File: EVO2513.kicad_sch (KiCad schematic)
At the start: 0 parts

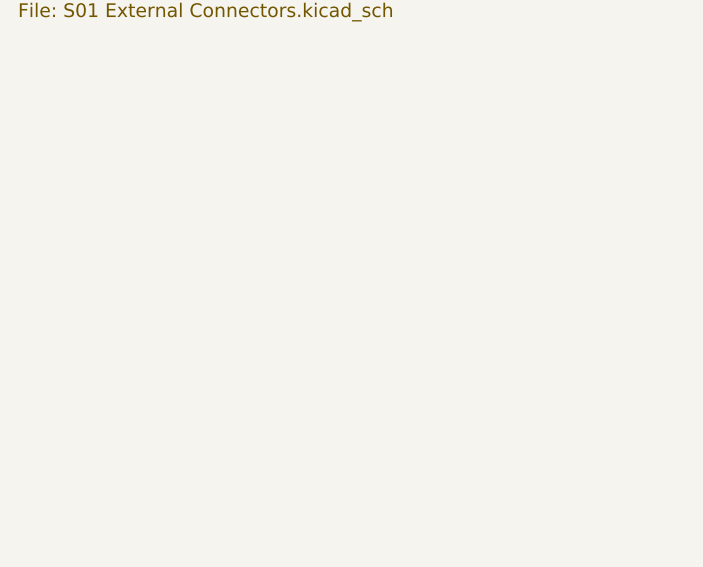
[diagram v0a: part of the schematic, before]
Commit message: Gate resistors placed, snubbers at the low-side FETs in EVM order, H1/H2/LOGO01 symbols
- R111-R114 (3R 0603) placed and routed next to the Q16-Q19 gates, each fed
  from In6 through a via in its driver-side pad.
- Snubbers reordered to match TI's LM51772EVM-HP (switch node -> C -> R -> GND)
  and moved to the low-side FETs: C39 on Q19's drain edge with R45 to GND,
  C35 on Q17's drain leads with R41 to GND, two In1 vias at each R GND pad.
  The top-copper SW1/SW2 pour lobes for the old positions are removed.
- H1, H2 (Mechanical:MountingHole_Pad, pin 1 to GND) and LOGO01 (pinless
  EVOSONIC_LOGO symbol) added to the root sheet and linked to their existing
  footprints, so Update PCB from Schematic no longer deletes them. The
  mounting-hole footprint is saved as MountingHole_3.2mm_Pad_7.4mm.
- ERC 0; DRC 0 unconnected, 0 parity, no courtyard overlaps.

Co-Authored-By: Claude Opus 5.5 <noreply@anthropic.com>
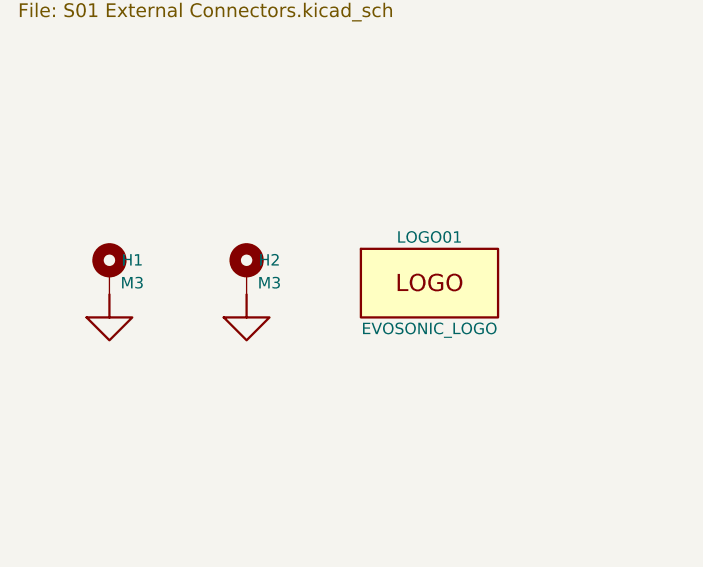
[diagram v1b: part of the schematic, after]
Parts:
- added H1, H2: M3, EVO2513-0_5_0-import-fps:MountingHole_3.2mm_Pad_7.4mm, symbol Mechanical:MountingHole_Pad
- added LOGO01: EVOSONIC_LOGO, EVO2513-0_5_0-import-fps:EVOSONIC_DNA_LOGO_390X600_MASK, symbol Lattech Systems:EVOSONIC_LOGO
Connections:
- new net GND: H1.1, H2.1

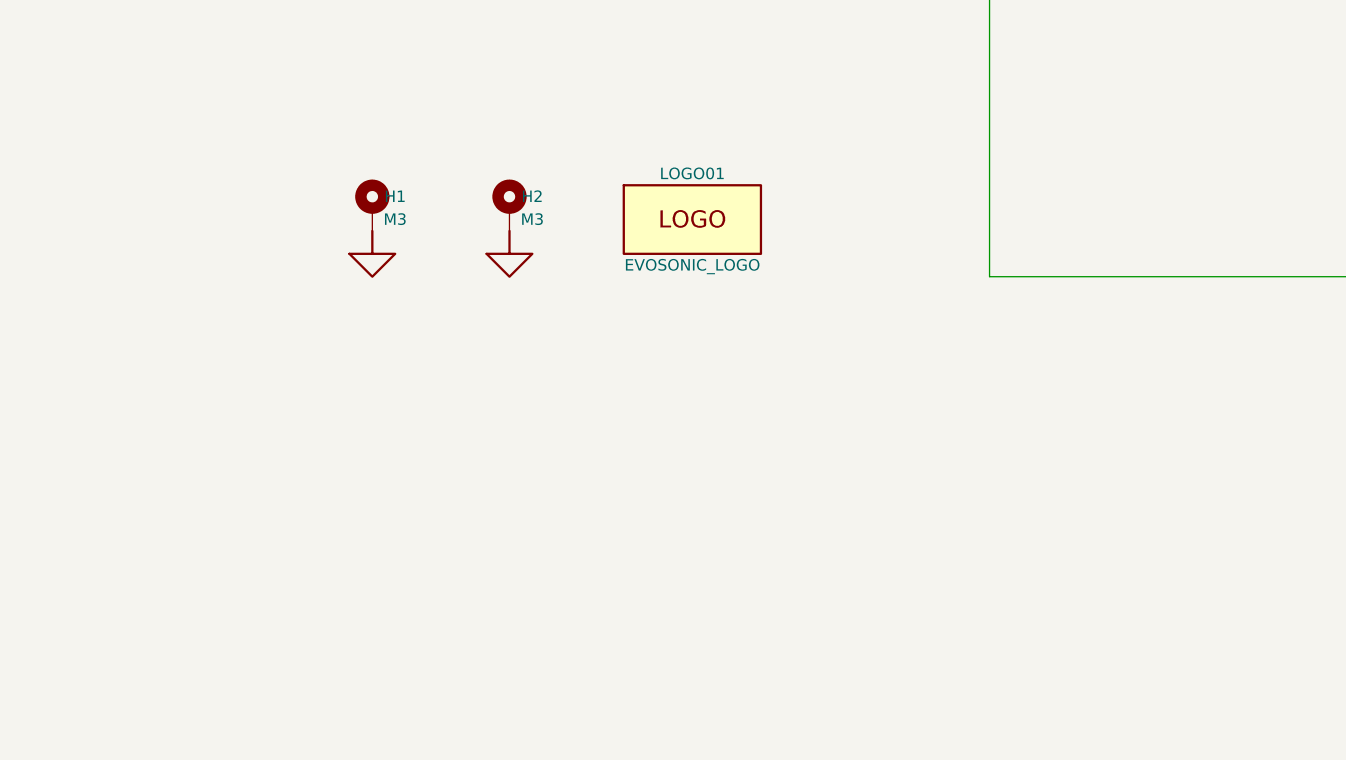
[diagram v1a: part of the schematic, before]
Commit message: Spacer thermal reliefs on the pad instead of keepout arcs
M1-M6: pad thermal relief, 2 mm spokes at 90 deg, 0.4 mm gap, set in the
library footprint as well as on the board. The four keepout arcs are
removed from the footprint. A DRC rule keeps other-net pours 0.45 mm from
M6, between the DCCHARGER and DCPATH pours.

Co-Authored-By: Claude Opus 5.5 <noreply@anthropic.com>
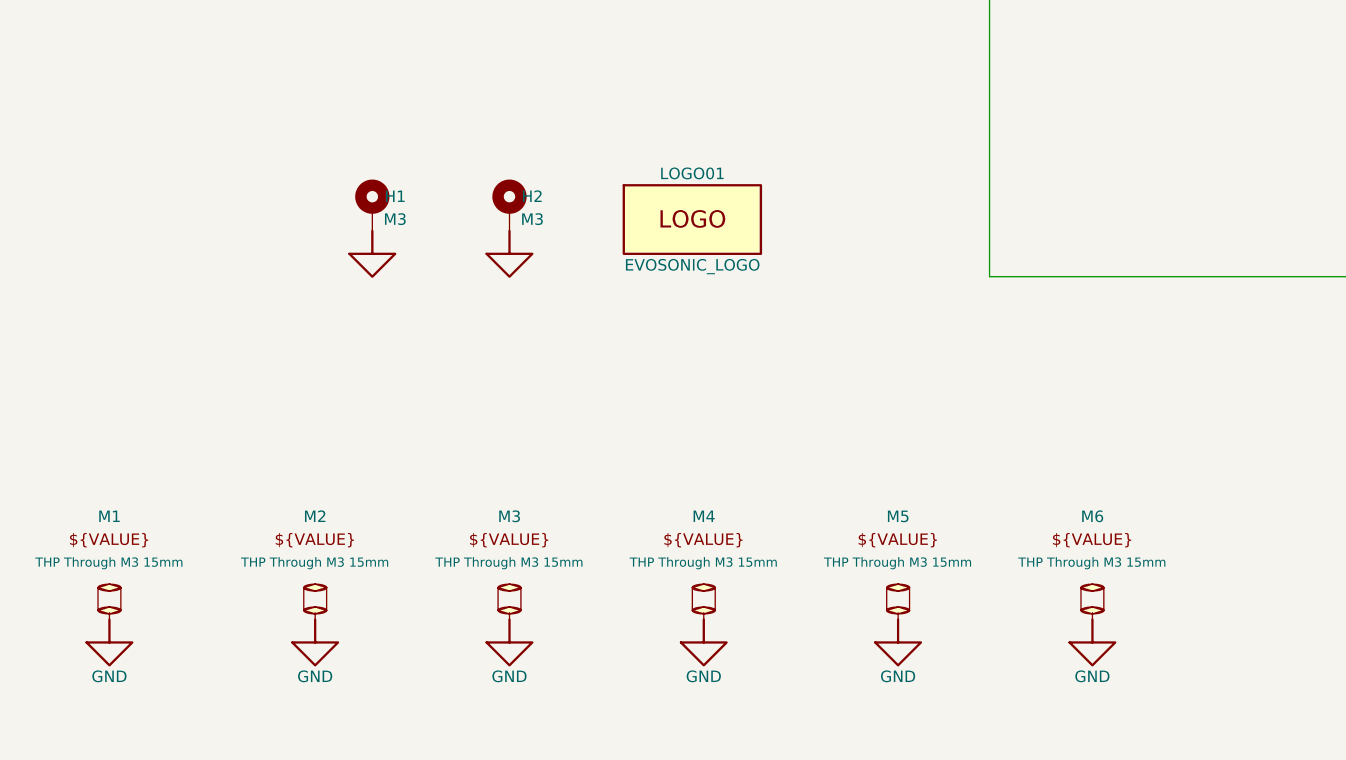
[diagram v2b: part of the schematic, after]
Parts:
- added M1, M2, M3, M4, M5, M6: 78614150960, EVO2513-0_5_0-import-fps:MECH SPACER WURTH 78614150960 THROUGH M3, symbol Lattech Systems:Mech Spacer Wurth 78614150960 Through M3 15mm
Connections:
- net GND: now also M1.1, M2.1, M3.1, M4.1, M5.1, M6.1
